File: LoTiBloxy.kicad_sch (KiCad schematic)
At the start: 0 parts

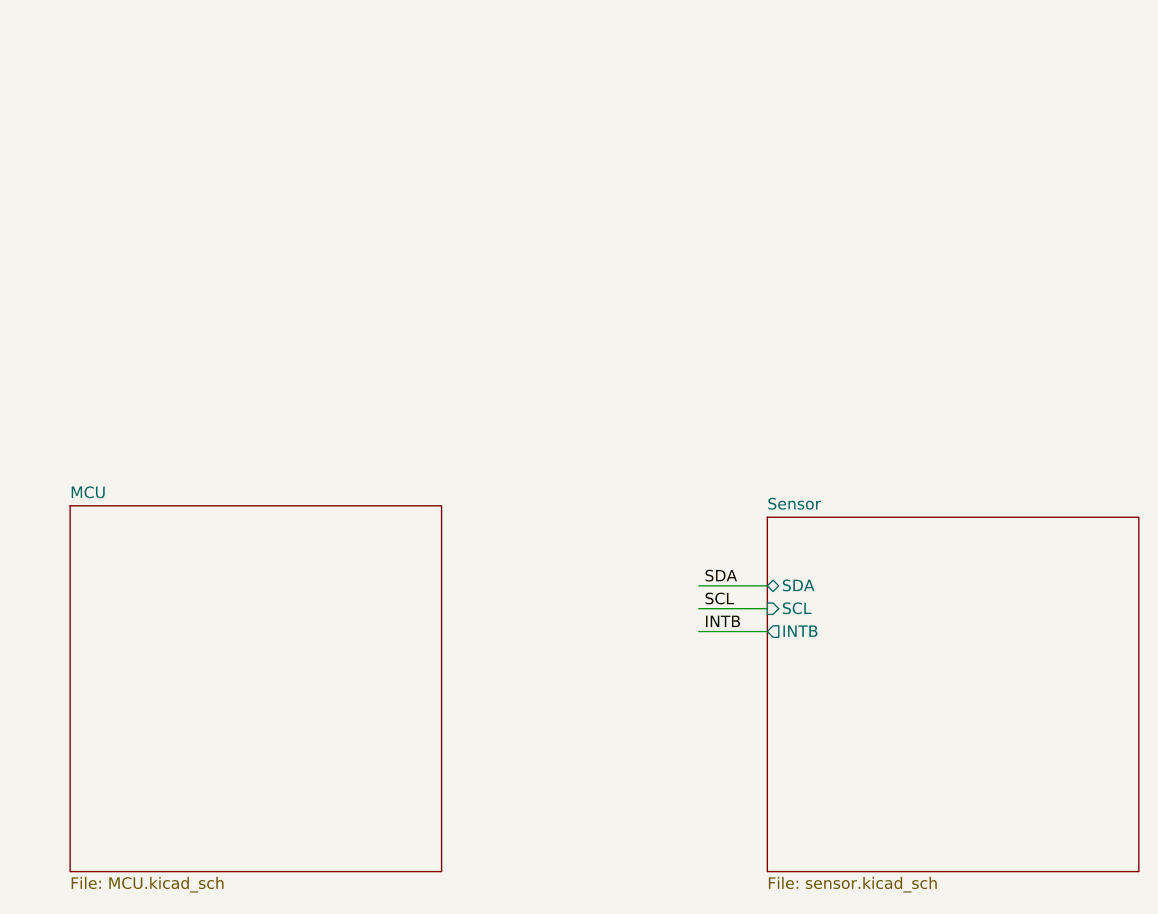
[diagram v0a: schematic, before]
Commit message: first finished schematic version of the MCU as well as sensor. starting out with schematic of the power related components
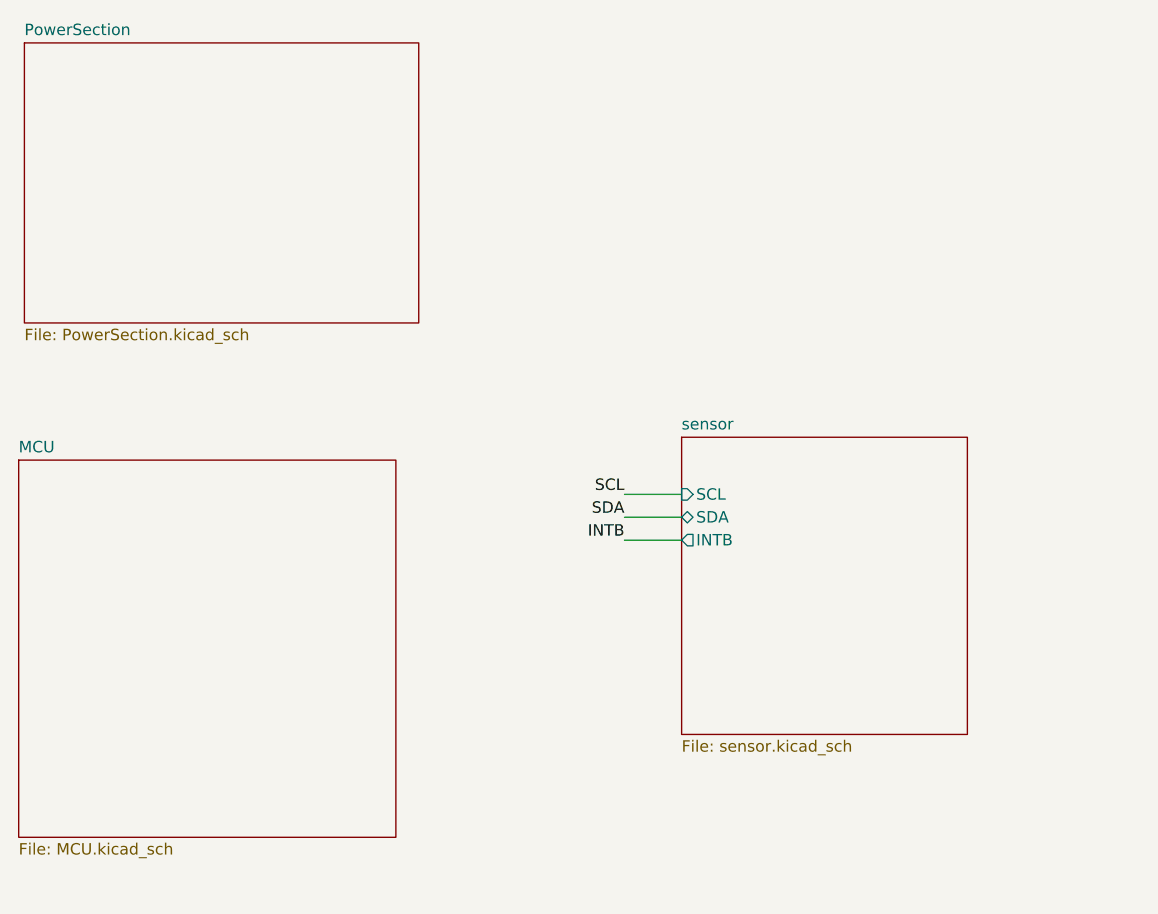
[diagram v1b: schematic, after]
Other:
- removed sheet Sensor
- added sheet PowerSection (PowerSection.kicad_sch)
- added sheet sensor (sensor.kicad_sch)
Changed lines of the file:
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@@
 	(wire
 		(pts
-			(xy 167.005 118.11) (xy 174.625 118.11)
+			(xy 158.75 102.87) (xy 165.1 102.87)
 		)
 		(stroke
@@
 	(wire
 		(pts
-			(xy 167.005 115.57) (xy 174.625 115.57)
+			(xy 158.75 105.41) (xy 165.1 105.41)
 		)
 		(stroke
@@
 	(wire
 		(pts
-			(xy 167.005 113.03) (xy 174.625 113.03)
+			(xy 158.75 107.95) (xy 165.1 107.95)
 		)
 		(stroke
@@
 	)
 	(label "SCL"
-		(at 167.64 115.57 0)
+		(at 158.75 102.87 180)
 		(effects
 			(font
 				(size 1.27 1.27)
 			)
-			(justify left bottom)
+			(justify right bottom)
 		)
 	)
 	(label "INTB"
-		(at 167.64 118.11 0)
+		(at 158.75 107.95 180)
 		(effects
 			(font
 				(size 1.27 1.27)
 			)
-			(justify left bottom)
+			(justify right bottom)
 		)
 	)
 	(label "SDA"
-		(at 167.64 113.03 0)
+		(at 158.75 105.41 180)
 		(effects
 			(font
 				(size 1.27 1.27)
 			)
-			(justify left bottom)
+			(justify right bottom)
 		)
 	)
 	(sheet
-		(at 174.625 105.41)
-		(size 41.275 39.37)
+		(at 92.075 52.705)
+		(size 43.815 31.115)
 		(exclude_from_sim no)
 		(in_bom yes)
@@
 			(color 0 0 0 0.0000)
 		)
-		(property "Sheetname" "Sensor"
-			(at 174.625 104.6984 0)
+		(property "Sheetname" "PowerSection"
+			(at 92.075 51.9934 0)
 			(effects
 				(font
@@
 			)
 		)
-		(property "Sheetfile" "sensor.kicad_sch"
-			(at 174.625 145.3646 0)
+		(property "Sheetfile" "PowerSection.kicad_sch"
+			(at 92.075 84.4046 0)
 			(effects
 				(font
@@
 				)
 				(justify left top)
-			)
-		)
-		(pin "SDA" bidirectional
-			(at 174.625 113.03 180)
-			(effects
-				(font
-					(size 1.27 1.27)
-				)
-				(justify left)
-			)
-		)
-		(pin "SCL" input
-			(at 174.625 115.57 180)
-			(effects
-				(font
-					(size 1.27 1.27)
-				)
-				(justify left)
-			)
-		)
-		(pin "INTB" output
-			(at 174.625 118.11 180)
-			(effects
-				(font
-					(size 1.27 1.27)
-				)
-				(justify left)
 			)
 		)
@@
 			(project "LoTiBloxy"
 				(path "/b00f58d9-17b8-4612-81ad-8f45c5b50f62"
-					(page "2")
+					(page "4")
 				)
 			)
@@
 	)
 	(sheet
-		(at 97.155 104.14)
-		(size 41.275 40.64)
+		(at 91.44 99.06)
+		(size 41.91 41.91)
 		(exclude_from_sim no)
 		(in_bom yes)
@@
 		)
 		(property "Sheetname" "MCU"
-			(at 97.155 103.4284 0)
+			(at 91.44 98.3484 0)
 			(effects
 				(font
@@
 		)
 		(property "Sheetfile" "MCU.kicad_sch"
-			(at 97.155 145.3646 0)
+			(at 91.44 141.5546 0)
 			(effects
 				(font
@@
 				)
 			)
+		)
+	)
+	(sheet
+		(at 165.1 96.52)
+		(size 31.75 33.02)
+		(exclude_from_sim no)
+		(in_bom yes)
+		(on_board yes)
+		(dnp no)
+		(fields_autoplaced yes)
+		(stroke
+			(width 0.1524)
+			(type solid)
+		)
+		(fill
+			(color 0 0 0 0.0000)
+		)
+		(property "Sheetname" "sensor"
+			(at 165.1 95.8084 0)
+			(effects
+				(font
+					(size 1.27 1.27)
+				)
+				(justify left bottom)
+			)
+		)
+		(property "Sheetfile" "sensor.kicad_sch"
+			(at 165.1 130.1246 0)
+			(effects
+				(font
+					(size 1.27 1.27)
+				)
+				(justify left top)
+			)
+		)
+		(pin "SCL" input
+			(at 165.1 102.87 180)
+			(effects
+				(font
+					(size 1.27 1.27)
+				)
+				(justify left)
+			)
+		)
+		(pin "SDA" bidirectional
+			(at 165.1 105.41 180)
+			(effects
+				(font
+					(size 1.27 1.27)
+				)
+				(justify left)
+			)
+		)
+		(pin "INTB" output
+			(at 165.1 107.95 180)
+			(effects
+				(font
+					(size 1.27 1.27)
+				)
+				(justify left)
+			)
+		)
+		(instances
+			(project "LoTiBloxy"
+				(path "/b00f58d9-17b8-4612-81ad-8f45c5b50f62"
+					(page "2")
+				)
+			)

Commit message: done with first version PowerSection of LoTiBloxy plus MCU plus sensor sheets. still have to add meaningfull comments to all schematic components. still have to make sure every symbol is associated to footprint. still have to perform ERC on what implemented.
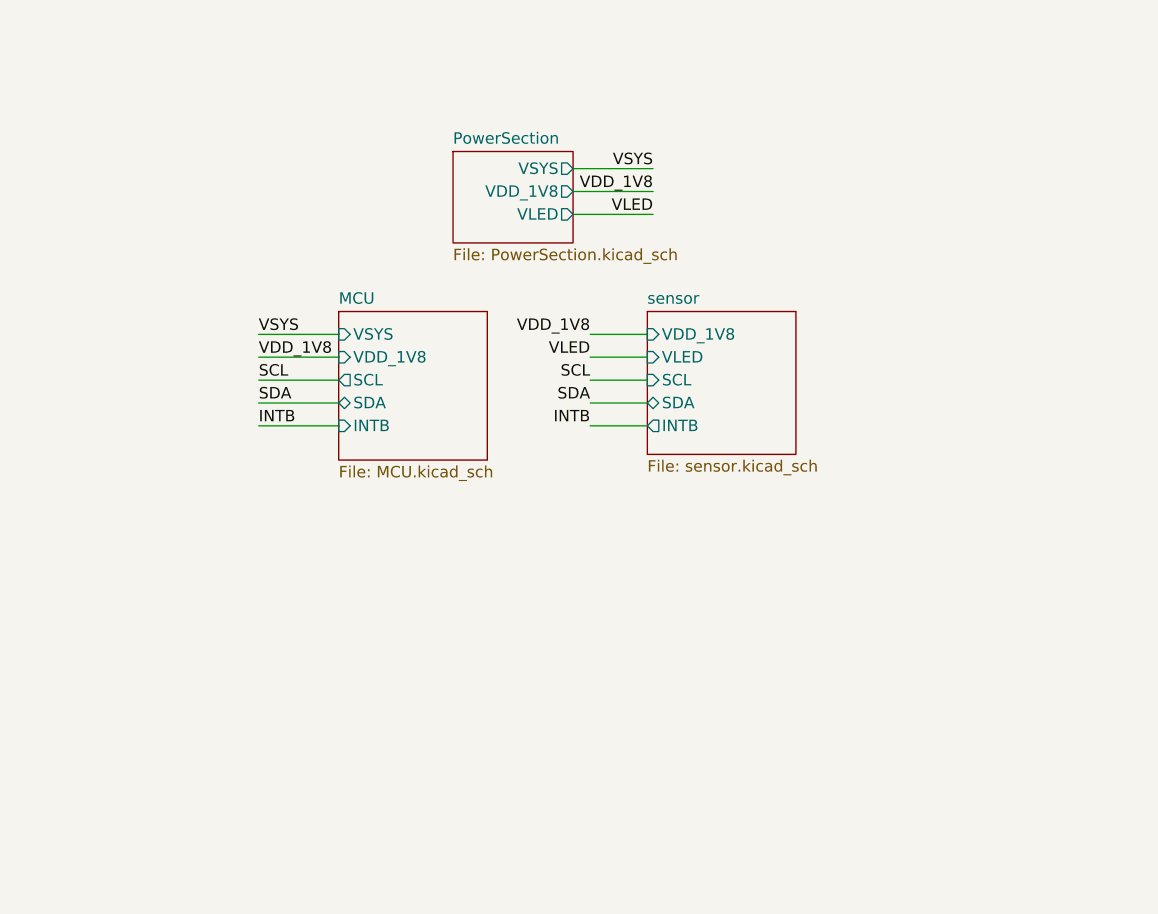
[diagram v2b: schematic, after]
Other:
- sheet MCU ports: added INTB, SCL, SDA, VDD_1V8, VSYS; removed none
- sheet PowerSection ports: added VDD_1V8, VLED, VSYS; removed none
- sheet sensor ports: added VDD_1V8, VLED; removed none
